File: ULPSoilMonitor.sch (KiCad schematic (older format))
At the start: 36 parts, among them J1 Conn_01x03_Male, J2 Conn_01x03_Male, J3 Conn_01x03_Male, J4 Conn_01x03_Male, J5 Conn_01x03_Male, J6 Conn_01x03_Male, J7 USB_B_Micro, Q1 BC807, Q2 MMDT3904, U1 ESP32-WROOM-32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

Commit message: fix cap unit of measure
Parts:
- C3: value 100μF -> 100nF
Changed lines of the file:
@@
 P 2600 1550
 F 0 "C3" H 2715 1596 50  0000 L CNN
-F 1 "100μF" H 2715 1505 50  0000 L CNN
+F 1 "100nF" H 2715 1505 50  0000 L CNN
 F 2 "Capacitors_SMD:C_0805" H 2638 1400 50  0001 C CNN
 F 3 "~" H 2600 1550 50  0001 C CNN

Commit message: update to use 18650 LiFePO4 cells
* connectors for one or two 18650 cells
* jumper to switch between battery & USB power
* add optional BME380
* reset push button
* more caps
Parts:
- removed C4: 100nF, Capacitors_SMD:C_0805, symbol Device:C
- removed J1, J2, J3, J4, J5, J6: Conn_01x03_Male, Pin_Headers:Pin_Header_Straight_1x03_Pitch2.54mm, symbol Connector:Conn_01x03_Male
- removed J7: USB_B_Micro, Connect:USB_Micro-B, symbol Connector:USB_B_Micro
- removed Q1: BC807, TO_SOT_Packages_SMD:SOT-23, symbol Transistor_BJT:BC807
- removed Q2: MMDT3904, TO_SOT_Packages_SMD:SOT-363_SC-70-6, symbol Transistor_BJT:MMDT3904
- removed R1, R11, R14, R5, R7, R9: 68k, Resistors_SMD:R_0805, symbol Device:R
- removed R10, R12, R15, R4, R6, R8: 30k, Resistors_SMD:R_0805, symbol Device:R
- removed R16: 3k9, Resistors_SMD:R_0805, symbol Device:R
- removed R17, R18: 10k, Resistors_SMD:R_0805, symbol Device:R
- removed R19, R20: 27R, Resistors_SMD:R_0805, symbol Device:R
- removed U2: FT231XS, Housings_SSOP:QSOP-20_3.9x8.7mm_Pitch0.635mm, symbol Interface_USB:FT231XS
- added C1: 470μF, Capacitor_SMD:CP_Elec_6.3x7.7, symbol Device:CP
- added C5: 330nF, Capacitor_SMD:C_0805_2012Metric, symbol Device:C
- added C6: 100nF, Capacitor_SMD:C_0805_2012Metric, symbol Device:C
- added JP1: Jumper_3_Bridged12, Connector_PinHeader_2.54mm:PinHeader_1x03_P2.54mm_Vertical, symbol Jumper:Jumper_3_Bridged12
- added SW1: RESET, Button_Switch_SMD:SW_SPST_FSMSM, symbol Switch:SW_Push
- added U2: UA7BM33, Package_TO_SOT_SMD:SOT-223-3_TabPin2, symbol Regulator_Linear:LM2937xMP
- BT1: footprint flobs-KiCad-footprints:BH321-2P -> flobs-KiCad-footprints:BatteryHolder_BHC-18650-1P-2P
- C2: renamed from C1; footprint Capacitors_SMD:C_0805 -> Capacitor_SMD:C_0805_2012Metric
- C3: renamed from C2; footprint Capacitors_SMD:C_0805 -> Capacitor_SMD:C_0805_2012Metric
- C4: renamed from C3; footprint Capacitors_SMD:C_0805 -> Capacitor_SMD:C_0805_2012Metric
- R1: renamed from R13; footprint Resistors_SMD:R_0805 -> Resistor_SMD:R_0805_2012Metric
- R2: value 30k -> 4k7; footprint Resistors_SMD:R_0805 -> Resistor_SMD:R_0805_2012Metric
- R3: value 68k -> 4k7; footprint Resistors_SMD:R_0805 -> Resistor_SMD:R_0805_2012Metric
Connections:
- net labels added: +3V3, SCL, SDA, VCC, VCC_SCALED
- net labels removed: BATT_SCALED, D+, D-, SENSOR0, SENSOR1, SENSOR2, SENSOR3, SENSOR4, SENSOR5, SENSOR_VCC
- wire segments 150 -> 95
- no-connect marks 30 -> 27
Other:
- moved on the sheet: BT1, C2, C3, C4, R1

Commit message: change USB to Serial chip, support charging
* exchanges FTDI FT231X for SILabs CP2102N
* adds MicroChip MCP73123 for LiFePO4 charging
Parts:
- removed C5: 330nF, Capacitor_SMD:C_0805_2012Metric, symbol Device:C
- removed C6: 100nF, Capacitor_SMD:C_0805_2012Metric, symbol Device:C
- removed JP1: Jumper_3_Bridged12, Connector_PinHeader_2.54mm:PinHeader_1x03_P2.54mm_Vertical, symbol Jumper:Jumper_3_Bridged12
- removed U2: UA7BM33, Package_TO_SOT_SMD:SOT-223-3_TabPin2, symbol Regulator_Linear:LM2937xMP
- added C?: 4.7μF, symbol Device:C
- added D?: CHARGING, symbol Device:LED
- added Q? (x2): MMDT3904, Package_TO_SOT_SMD:SOT-363_SC-70-6, symbol Transistor_BJT:MMDT3904
- added Q?: BC817, Package_TO_SOT_SMD:SOT-23, symbol Transistor_BJT:BC817
- added R?: 1k, symbol Device:R
- added R?: 2k37, symbol Device:R
- added R?: 3k9, symbol Device:R
- added U?: MCP73123, Package_DFN_QFN:DFN-10-1EP_3x3mm_P0.5mm_EP1.65x2.38mm_ThermalVias, symbol flobs-KiCad-lib:MCP73123
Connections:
- net labels added: CHR0, CHR1, CHREN, PROG
- net labels removed: +3V3
- wire segments 95 -> 117
- no-connect marks 27 -> 34

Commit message: update drawing to 882a528a10f6fb48f6454efd446c1280f51ad1f8
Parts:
- C5: renamed from C?; footprint (none) -> Capacitor_SMD:C_0805_2012Metric
- D1: renamed from D?; footprint (none) -> LED_SMD:LED_0805_2012Metric
- R23, R24, R25: renamed from R?; footprint (none) -> Resistor_SMD:R_0805_2012Metric
- U2: renamed from U?; footprint Package_DFN_QFN:DFN-10-1EP_3x3mm_P0.5mm_EP1.65x2.38mm_ThermalVias -> Package_DFN_QFN:DFN-10-1EP_3x3mm_P0.5mm_EP1.65x2.38mm
- gave numbers to parts that had none: 2
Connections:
- wire segments 117 -> 119
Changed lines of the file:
@@
 Sheet 1 5
 Title "ULPSoilMonitor"
-Date "2020-05-16"
-Rev "v2.0"
+Date "2020-06-26"
+Rev "v2.1"
 Comp "Flobs"
 Comment1 ""
@@
 Wire Wire Line
 	2350 1050 2350 1150
-Wire Wire Line
-	2150 1050 2150 900
 Connection ~ 2150 1050
 Wire Wire Line
@@
 	5700 1250 5850 1250
 Wire Wire Line
-	1950 1050 1500 1050
+	1950 1050 1750 1050
 Wire Wire Line
 	1500 1050 1500 1150
@@
 	4500 5300 4600 5300
 $Comp
-L flobs-KiCad-lib:MCP73123 U?
+L flobs-KiCad-lib:MCP73123 U2
 U 1 1 5EFBF713
 P 7400 5400
-F 0 "U?" H 7400 5915 50  0000 C CNN
+F 0 "U2" H 7400 5915 50  0000 C CNN
 F 1 "MCP73123" H 7400 5824 50  0000 C CNN
-F 2 "Package_DFN_QFN:DFN-10-1EP_3x3mm_P0.5mm_EP1.65x2.38mm_ThermalVias" H 7050 6200 50  0001 C CNN
+F 2 "Package_DFN_QFN:DFN-10-1EP_3x3mm_P0.5mm_EP1.65x2.38mm" H 7050 6200 50  0001 C CNN
 F 3 "" H 7050 6200 50  0001 C CNN
 	1    7400 5400
@@
 $EndComp
 $Comp
-L power:GND #PWR?
+L power:GND #PWR0101
 U 1 1 5EFC114A
 P 7400 6250
-F 0 "#PWR?" H 7400 6000 50  0001 C CNN
+F 0 "#PWR0101" H 7400 6000 50  0001 C CNN
 F 1 "GND" H 7405 6077 50  0000 C CNN
 F 2 "" H 7400 6250 50  0001 C CNN
@@
 $EndComp
 $Comp
-L power:GND #PWR?
+L power:GND #PWR0102
 U 1 1 5EFC14F0
 P 8050 5800
-F 0 "#PWR?" H 8050 5550 50  0001 C CNN
+F 0 "#PWR0102" H 8050 5550 50  0001 C CNN
 F 1 "GND" H 8055 5627 50  0000 C CNN
 F 2 "" H 8050 5800 50  0001 C CNN
@@
 Connection ~ 8050 5450
 $Comp
-L power:+BATT #PWR?
+L power:+BATT #PWR0103
 U 1 1 5EFC7B48
 P 6550 5000
-F 0 "#PWR?" H 6550 4850 50  0001 C CNN
+F 0 "#PWR0103" H 6550 4850 50  0001 C CNN
 F 1 "+BATT" H 6565 5173 50  0000 C CNN
 F 2 "" H 6550 5000 50  0001 C CNN
@@
 $EndComp
 $Comp
-L power:VBUS #PWR?
+L power:VBUS #PWR0104
 U 1 1 5EFC869F
 P 6750 4900
-F 0 "#PWR?" H 6750 4750 50  0001 C CNN
+F 0 "#PWR0104" H 6750 4750 50  0001 C CNN
 F 1 "VBUS" H 6765 5073 50  0000 C CNN
 F 2 "" H 6750 4900 50  0001 C CNN
@@
 	7900 5450 8050 5450
 $Comp
-L Device:LED D?
+L Device:LED D1
 U 1 1 5EFE3865
 P 8300 5350
-F 0 "D?" V 8339 5232 50  0000 R CNN
+F 0 "D1" V 8339 5232 50  0000 R CNN
 F 1 "CHARGING" V 8248 5232 50  0000 R CNN
-F 2 "" H 8300 5350 50  0001 C CNN
+F 2 "LED_SMD:LED_0805_2012Metric" H 8300 5350 50  0001 C CNN
 F 3 "~" H 8300 5350 50  0001 C CNN
 	1    8300 5350
@@
 $EndComp
 $Comp
-L Device:R R?
+L Device:R R23
 U 1 1 5EFE4E96
 P 8300 4900
-F 0 "R?" H 8370 4946 50  0000 L CNN
+F 0 "R23" H 8370 4946 50  0000 L CNN
 F 1 "1k" H 8370 4855 50  0000 L CNN
-F 2 "" V 8230 4900 50  0001 C CNN
+F 2 "Resistor_SMD:R_0805_2012Metric" V 8230 4900 50  0001 C CNN
 F 3 "~" H 8300 4900 50  0001 C CNN
 	1    8300 4900
@@
 	8300 5200 8300 5050
 $Comp
-L power:VBUS #PWR?
+L power:VBUS #PWR0105
 U 1 1 5EFEC5B1
 P 8300 4650
-F 0 "#PWR?" H 8300 4500 50  0001 C CNN
+F 0 "#PWR0105" H 8300 4500 50  0001 C CNN
 F 1 "VBUS" H 8315 4823 50  0000 C CNN
 F 2 "" H 8300 4650 50  0001 C CNN
@@
 	8300 4750 8300 4650
 $Comp
-L Device:C C?
+L Device:C C5
 U 1 1 5EFF0D8F
 P 6550 5900
-F 0 "C?" H 6665 5946 50  0000 L CNN
+F 0 "C5" H 6665 5946 50  0000 L CNN
 F 1 "4.7μF" H 6665 5855 50  0000 L CNN
-F 2 "" H 6588 5750 50  0001 C CNN
+F 2 "Capacitor_SMD:C_0805_2012Metric" H 6588 5750 50  0001 C CNN
 F 3 "~" H 6550 5900 50  0001 C CNN
 	1    6550 5900
@@
 	6550 6050 6550 6250
 $Comp
-L power:GND #PWR?
+L power:GND #PWR0106
 U 1 1 5EFF8A21
 P 6550 6250
-F 0 "#PWR?" H 6550 6000 50  0001 C CNN
+F 0 "#PWR0106" H 6550 6000 50  0001 C CNN
 F 1 "GND" H 6555 6077 50  0000 C CNN
 F 2 "" H 6550 6250 50  0001 C CNN
@@
 	7900 5150 8000 5150
 $Comp
-L Device:R R?
+L Device:R R25
 U 1 1 5F015CC3
 P 9900 5350
-F 0 "R?" H 9970 5396 50  0000 L CNN
+F 0 "R25" H 9970 5396 50  0000 L CNN
 F 1 "2k37" H 9970 5305 50  0000 L CNN
-F 2 "" V 9830 5350 50  0001 C CNN
+F 2 "Resistor_SMD:R_0805_2012Metric" V 9830 5350 50  0001 C CNN
 F 3 "~" H 9900 5350 50  0001 C CNN
 	1    9900 5350
@@
 $EndComp
 $Comp
-L Transistor_BJT:MMDT3904 Q?
+L Transistor_BJT:MMDT3904 Q4
 U 1 1 5F018C0F
 P 9500 5600
-F 0 "Q?" H 9691 5646 50  0000 L CNN
+F 0 "Q4" H 9691 5646 50  0000 L CNN
 F 1 "MMDT3904" H 9691 5555 50  0000 L CNN
 F 2 "Package_TO_SOT_SMD:SOT-363_SC-70-6" H 9700 5700 50  0001 C CNN
@@
 $EndComp
 $Comp
-L Transistor_BJT:MMDT3904 Q?
+L Transistor_BJT:MMDT3904 Q4
 U 2 1 5F019AA5
 P 10000 5900
-F 0 "Q?" H 10191 5946 50  0000 L CNN
+F 0 "Q4" H 10191 5946 50  0000 L CNN
 F 1 "MMDT3904" H 10191 5855 50  0000 L CNN
 F 2 "Package_TO_SOT_SMD:SOT-363_SC-70-6" H 10200 6000 50  0001 C CNN
@@
 CHR0
 $Comp
-L Device:R R?
+L Device:R R24
 U 1 1 5F02346F
 P 9400 5150
-F 0 "R?" H 9470 5196 50  0000 L CNN
+F 0 "R24" H 9470 5196 50  0000 L CNN
 F 1 "3k9" H 9470 5105 50  0000 L CNN
-F 2 "" V 9330 5150 50  0001 C CNN
+F 2 "Resistor_SMD:R_0805_2012Metric" V 9330 5150 50  0001 C CNN
 F 3 "~" H 9400 5150 50  0001 C CNN
 	1    9400 5150
@@
 CHR1
 $Comp
-L power:GND #PWR?
+L power:GND #PWR0107
 U 1 1 5F02E788
 P 9650 6300
-F 0 "#PWR?" H 9650 6050 50  0001 C CNN
+F 0 "#PWR0107" H 9650 6050 50  0001 C CNN
 F 1 "GND" H 9655 6127 50  0000 C CNN
 F 2 "" H 9650 6300 50  0001 C CNN
@@
 	9700 5600 10300 5600
 $Comp
-L Transistor_BJT:BC817 Q?
+L Transistor_BJT:BC817 Q3
 U 1 1 5F0D63E8
 P 9750 4600
-F 0 "Q?" H 9941 4646 50  0000 L CNN
+F 0 "Q3" H 9941 4646 50  0000 L CNN
 F 1 "BC817" H 9941 4555 50  0000 L CNN
 F 2 "Package_TO_SOT_SMD:SOT-23" H 9950 4525 50  0001 L CIN
@@
 Wire Wire Line
 	9950 4600 10050 4600
+$Comp
+L power:+BATT #PWR0112
+U 1 1 5EF7A415
+P 1750 900
+F 0 "#PWR0112" H 1750 750 50  0001 C CNN
+F 1 "+BATT" H 1765 1073 50  0000 C CNN
+F 2 "" H 1750 900 50  0001 C CNN
+F 3 "" H 1750 900 50  0001 C CNN
+	1    1750 900
+	1    0    0    -1
+$EndComp
+Wire Wire Line
+	2150 900  2150 1050
+Wire Wire Line
+	1750 900  1750 1050
+Connection ~ 1750 1050
+Wire Wire Line
+	1750 1050 1500 1050
 $EndSCHEMATC

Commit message: Add JCLPCB/LCSC part numbers
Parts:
- C1: LCSC (none) -> C335982
- C2: LCSC (none) -> C45783
- C3, C4: LCSC (none) -> C49678
- C5: LCSC (none) -> C1779
- D1: LCSC (none) -> C84256
- Q3: LCSC (none) -> C118725
- Q4: LCSC (none) -> C155305
- R1: LCSC (none) -> C17414
- R2, R3: LCSC (none) -> C17673
- R23: LCSC (none) -> C17513
- R24: LCSC (none) -> C17614
- R25: LCSC (none) -> C17523
- SW1: LCSC (none) -> C354943
- U1: symbol RF_Module:ESP32-WROOM-32 -> ULPSoilMonitor-rescue:ESP32-WROOM-32-RF_Module; LCSC (none) -> C473012
- U2: symbol flobs-KiCad-lib:MCP73123 -> ULPSoilMonitor-rescue:MCP73123-flobs-KiCad-lib
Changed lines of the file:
@@
 EESchema Schematic File Version 4
+LIBS:ULPSoilMonitor-cache
 EELAYER 30 0
 EELAYER END
@@
 F 2 "Resistor_SMD:R_0805_2012Metric" V 3530 2750 50  0001 C CNN
 F 3 "~" H 3600 2750 50  0001 C CNN
+F 4 "C17673" H 3600 2750 50  0001 C CNN "LCSC"
 	1    3600 2750
 	0    1    1    0
@@
 F 2 "Resistor_SMD:R_0805_2012Metric" V 3530 2950 50  0001 C CNN
 F 3 "~" H 3600 2950 50  0001 C CNN
+F 4 "C17673" H 3600 2950 50  0001 C CNN "LCSC"
 	1    3600 2950
 	0    1    1    0
@@
 F 2 "Capacitor_SMD:CP_Elec_6.3x7.7" H 1538 1150 50  0001 C CNN
 F 3 "~" H 1500 1300 50  0001 C CNN
+F 4 "C335982" H 1500 1300 50  0001 C CNN "LCSC"
 	1    1500 1300
 	1    0    0    -1
@@
 F 2 "Capacitor_SMD:C_0805_2012Metric" H 3038 1400 50  0001 C CNN
 F 3 "~" H 3000 1550 50  0001 C CNN
+F 4 "C49678" H 3000 1550 50  0001 C CNN "LCSC"
 	1    3000 1550
 	1    0    0    -1
@@
 F 2 "Resistor_SMD:R_0805_2012Metric" V 2930 1050 50  0001 C CNN
 F 3 "~" H 3000 1050 50  0001 C CNN
+F 4 "C17414" H 3000 1050 50  0001 C CNN "LCSC"
 	1    3000 1050
 	1    0    0    -1
@@
 F 2 "Capacitor_SMD:C_0805_2012Metric" H 2388 1150 50  0001 C CNN
 F 3 "~" H 2350 1300 50  0001 C CNN
+F 4 "C49678" H 2350 1300 50  0001 C CNN "LCSC"
 	1    2350 1300
 	1    0    0    -1
@@
 F 2 "Capacitor_SMD:C_0805_2012Metric" H 1988 1150 50  0001 C CNN
 F 3 "~" H 1950 1300 50  0001 C CNN
+F 4 "C45783" H 1950 1300 50  0001 C CNN "LCSC"
 	1    1950 1300
 	1    0    0    -1
@@
 $EndComp
 $Comp
-L RF_Module:ESP32-WROOM-32 U1
+L ULPSoilMonitor-rescue:ESP32-WROOM-32-RF_Module U1
 U 1 1 5E9ED41E
 P 5100 2450
@@
 F 2 "RF_Module:ESP32-WROOM-32" H 5100 950 50  0001 C CNN
 F 3 "https://www.espressif.com/sites/default/files/documentation/esp32-wroom-32_datasheet_en.pdf" H 4800 2500 50  0001 C CNN
+F 4 "C473012" H 5100 2450 50  0001 C CNN "LCSC"
 	1    5100 2450
 	1    0    0    -1
@@
 F 2 "Button_Switch_SMD:SW_SPST_FSMSM" H 6650 1500 50  0001 C CNN
 F 3 "~" H 6650 1500 50  0001 C CNN
+F 4 "C354943" V 6650 1300 50  0001 C CNN "LCSC"
 	1    6650 1300
 	0    1    1    0
@@
 	4500 5300 4600 5300
 $Comp
-L flobs-KiCad-lib:MCP73123 U2
+L ULPSoilMonitor-rescue:MCP73123-flobs-KiCad-lib U2
 U 1 1 5EFBF713
 P 7400 5400
@@
 F 2 "LED_SMD:LED_0805_2012Metric" H 8300 5350 50  0001 C CNN
 F 3 "~" H 8300 5350 50  0001 C CNN
+F 4 "C84256" H 8300 5350 50  0001 C CNN "LCSC"
 	1    8300 5350
 	0    -1   -1   0
@@
 F 2 "Resistor_SMD:R_0805_2012Metric" V 8230 4900 50  0001 C CNN
 F 3 "~" H 8300 4900 50  0001 C CNN
+F 4 "C17513" H 8300 4900 50  0001 C CNN "LCSC"
 	1    8300 4900
 	1    0    0    -1
@@
 F 2 "Capacitor_SMD:C_0805_2012Metric" H 6588 5750 50  0001 C CNN
 F 3 "~" H 6550 5900 50  0001 C CNN
+F 4 "C1779" H 6550 5900 50  0001 C CNN "LCSC"
 	1    6550 5900
 	1    0    0    -1
@@
 F 2 "Resistor_SMD:R_0805_2012Metric" V 9830 5350 50  0001 C CNN
 F 3 "~" H 9900 5350 50  0001 C CNN
+F 4 "C17523" H 9900 5350 50  0001 C CNN "LCSC"
 	1    9900 5350
 	1    0    0    -1
@@
 F 2 "Package_TO_SOT_SMD:SOT-363_SC-70-6" H 9700 5700 50  0001 C CNN
 F 3 "http://www.diodes.com/_files/datasheets/ds30088.pdf" H 9500 5600 50  0001 C CNN
+F 4 "C155305" H 9500 5600 50  0001 C CNN "LCSC"
 	1    9500 5600
 	-1   0    0    -1
@@
 F 2 "Package_TO_SOT_SMD:SOT-363_SC-70-6" H 10200 6000 50  0001 C CNN
 F 3 "http://www.diodes.com/_files/datasheets/ds30088.pdf" H 10000 5900 50  0001 C CNN
+F 4 "C155305" H 10000 5900 50  0001 C CNN "LCSC"
 	2    10000 5900
 	-1   0    0    -1
@@
 F 2 "Resistor_SMD:R_0805_2012Metric" V 9330 5150 50  0001 C CNN
 F 3 "~" H 9400 5150 50  0001 C CNN
+F 4 "C17614" H 9400 5150 50  0001 C CNN "LCSC"
 	1    9400 5150
 	1    0    0    -1
@@
 F 2 "Package_TO_SOT_SMD:SOT-23" H 9950 4525 50  0001 L CIN
 F 3 "http://www.fairchildsemi.com/ds/BC/BC817.pdf" H 9750 4600 50  0001 L CNN
+F 4 "C118725" H 9750 4600 50  0001 C CNN "LCSC"
 	1    9750 4600
 	-1   0    0    -1

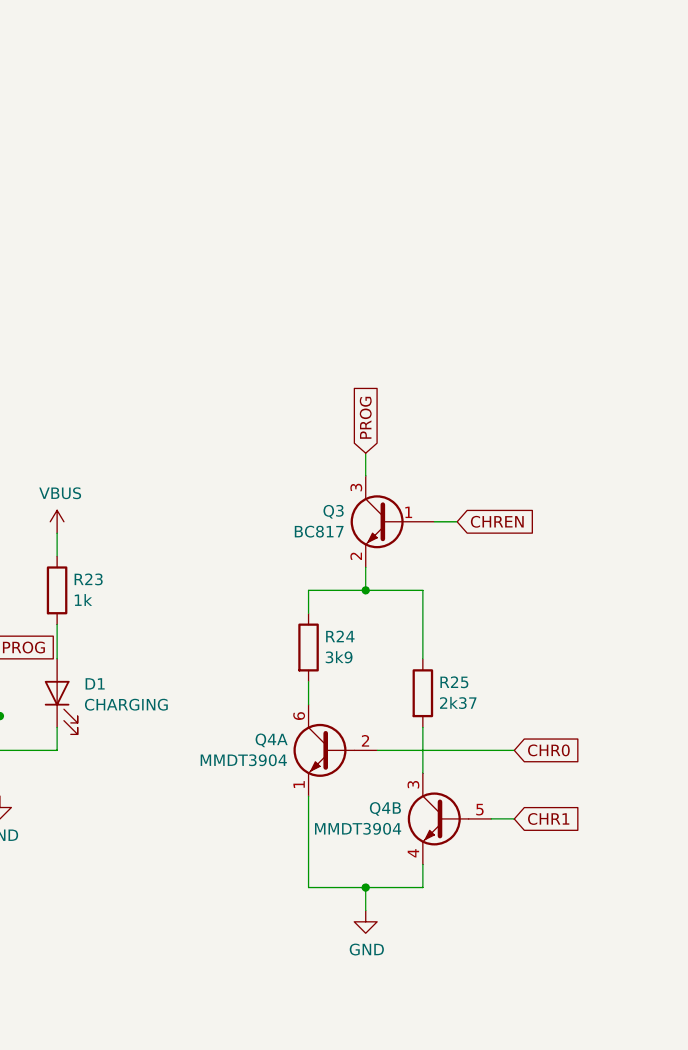
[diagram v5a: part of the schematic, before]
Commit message: Set USB-serial DNP
Disable USB-serial
Add switches for LiFePo charger PROG setting
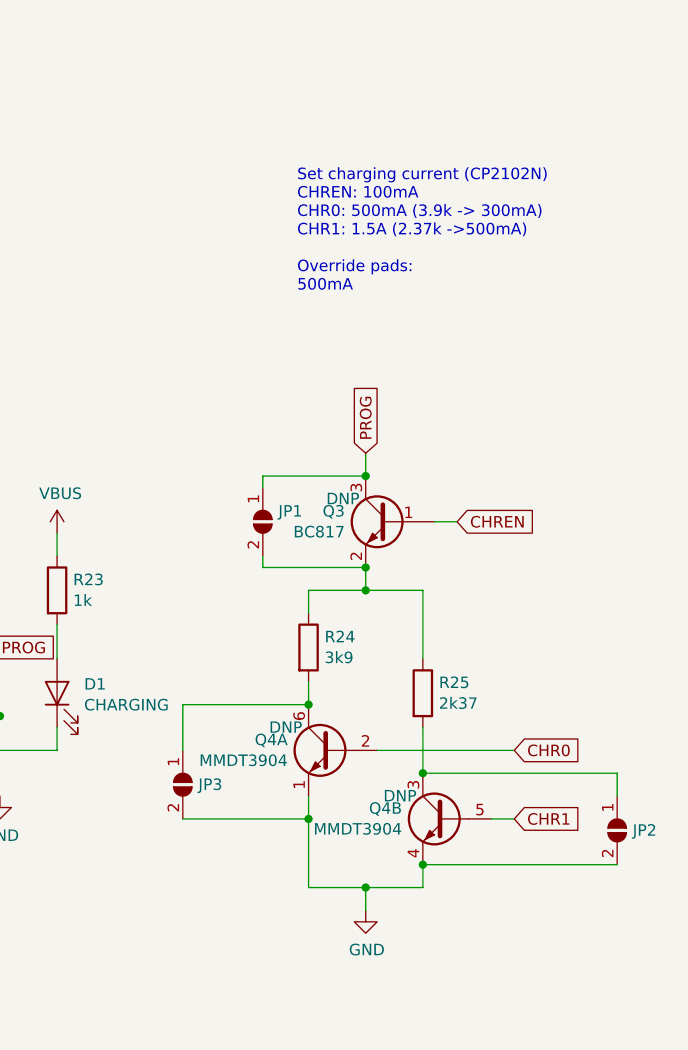
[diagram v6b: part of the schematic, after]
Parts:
- added JP1, JP2, JP3: SolderJumper_2_Open, Jumper:SolderJumper-2_P1.3mm_Open_RoundedPad1.0x1.5mm, symbol 0-GIE_SMD_Jumpers:SolderJumper_2_Open
- Q3, Q4: DNP (none) -> DNP
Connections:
- net -BATT: now also JP2.2 (B), JP3.2 (B)
- net PROG: now also JP1.1 (A)
- net at Q3.2 (E), R24.1, R25.1: now also JP1.2 (B)
- net at Q4.3 (C2), R25.2: now also JP2.1 (A)
- net at Q4.6 (C1), R24.2: now also JP3.1 (A)
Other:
- note added: "Set charging current (CP2102N)\nCHREN: 100mA\nCHR0: 500mA (3.9k -> 300mA)\nCHR1: 1.5A (2.37k ->500mA)\n\nOverride pads: \n500mA"
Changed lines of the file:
@@
 F 3 "http://www.diodes.com/_files/datasheets/ds30088.pdf" H 9500 5600 50  0001 C CNN
 F 4 "C155305" H 9500 5600 50  0001 C CNN "LCSC"
+F 5 "DNP" H 9700 5700 50  0000 C CNN "DNP"
 	1    9500 5600
 	-1   0    0    -1
@@
 F 3 "http://www.diodes.com/_files/datasheets/ds30088.pdf" H 10000 5900 50  0001 C CNN
 F 4 "C155305" H 10000 5900 50  0001 C CNN "LCSC"
+F 5 "DNP" H 10200 6000 50  0000 C CNN "DNP"
 	2    10000 5900
 	-1   0    0    -1
@@
 Text GLabel 10300 5600 2    50   Input ~ 0
 CHR0
-$Comp
-L Device:R R24
-U 1 1 5F02346F
-P 9400 5150
-F 0 "R24" H 9470 5196 50  0000 L CNN
-F 1 "3k9" H 9470 5105 50  0000 L CNN
-F 2 "Resistor_SMD:R_0805_2012Metric" V 9330 5150 50  0001 C CNN
-F 3 "~" H 9400 5150 50  0001 C CNN
-F 4 "C17614" H 9400 5150 50  0001 C CNN "LCSC"
-	1    9400 5150
-	1    0    0    -1
-$EndComp
 Text GLabel 10300 5900 2    50   Input ~ 0
 CHR1
@@
 $EndComp
 Wire Wire Line
-	9400 5800 9400 6200
+	9400 5800 9400 5900
 Wire Wire Line
 	9400 6200 9650 6200
@@
 F 3 "http://www.fairchildsemi.com/ds/BC/BC817.pdf" H 9750 4600 50  0001 L CNN
 F 4 "C118725" H 9750 4600 50  0001 C CNN "LCSC"
+F 5 "DNP" H 9950 4700 50  0000 C CNN "DNP"
 	1    9750 4600
 	-1   0    0    -1
@@
 Wire Wire Line
 	1750 1050 1500 1050
+Text Notes 9350 3600 0    50   ~ 0
+Set charging current (CP2102N)\nCHREN: 100mA\nCHR0: 500mA (3.9k -> 300mA)\nCHR1: 1.5A (2.37k ->500mA)\n\nOverride pads: \n500mA
+$Comp
+L 0-GIE_SMD_Jumpers:SolderJumper_2_Open JP1
+U 1 1 605B68DB
+P 9200 4600
+F 0 "JP1" V 9154 4668 50  0000 L CNN
+F 1 "SolderJumper_2_Open" V 9245 4668 50  0001 L CNN
+F 2 "Jumper:SolderJumper-2_P1.3mm_Open_RoundedPad1.0x1.5mm" H 9200 4600 50  0001 C CNN
+F 3 "~" H 9200 4600 50  0001 C CNN
+	1    9200 4600
+	0    1    1    0
+$EndComp
+$Comp
+L 0-GIE_SMD_Jumpers:SolderJumper_2_Open JP2
+U 1 1 605B8584
+P 10750 5950
+F 0 "JP2" V 10750 6018 50  0000 L CNN
+F 1 "SolderJumper_2_Open" V 10795 6018 50  0001 L CNN
+F 2 "Jumper:SolderJumper-2_P1.3mm_Open_RoundedPad1.0x1.5mm" H 10750 5950 50  0001 C CNN
+F 3 "~" H 10750 5950 50  0001 C CNN
+	1    10750 5950
+	0    1    1    0
+$EndComp
+Wire Wire Line
+	9650 4400 9200 4400
+Wire Wire Line
+	9200 4400 9200 4450
+Connection ~ 9650 4400
+Wire Wire Line
+	9200 4750 9200 4800
+Wire Wire Line
+	9200 4800 9650 4800
+Connection ~ 9650 4800
+Wire Wire Line
+	10750 5800 10750 5700
+Wire Wire Line
+	10750 5700 9900 5700
+Connection ~ 9900 5700
+Wire Wire Line
+	9900 6100 10750 6100
+Connection ~ 9900 6100
+$Comp
+L Device:R R24
+U 1 1 5F02346F
+P 9400 5150
+F 0 "R24" H 9470 5196 50  0000 L CNN
+F 1 "3k9" H 9470 5105 50  0000 L CNN
+F 2 "Resistor_SMD:R_0805_2012Metric" V 9330 5150 50  0001 C CNN
+F 3 "~" H 9400 5150 50  0001 C CNN
+F 4 "C17614" H 9400 5150 50  0001 C CNN "LCSC"
+	1    9400 5150
+	1    0    0    -1
+$EndComp
+$Comp
+L 0-GIE_SMD_Jumpers:SolderJumper_2_Open JP3
+U 1 1 605D5828
+P 8850 5750
+F 0 "JP3" V 8850 5818 50  0000 L CNN
+F 1 "SolderJumper_2_Open" V 8895 5818 50  0001 L CNN
+F 2 "Jumper:SolderJumper-2_P1.3mm_Open_RoundedPad1.0x1.5mm" H 8850 5750 50  0001 C CNN
+F 3 "~" H 8850 5750 50  0001 C CNN
+	1    8850 5750
+	0    1    1    0
+$EndComp
+Wire Wire Line
+	8850 5600 8850 5400
+Wire Wire Line
+	8850 5400 9400 5400
+Connection ~ 9400 5400
+Wire Wire Line
+	8850 5900 9400 5900
+Connection ~ 9400 5900
+Wire Wire Line
+	9400 5900 9400 6200
 $EndSCHEMATC

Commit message: Update jumper names
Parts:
- JP1: value SolderJumper_2_Open -> Charg_enable
- JP2: value SolderJumper_2_Open -> Charge_500mA
- JP3: value SolderJumper_2_Open -> Charge_300mA
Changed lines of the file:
@@
 P 9200 4600
 F 0 "JP1" V 9154 4668 50  0000 L CNN
-F 1 "SolderJumper_2_Open" V 9245 4668 50  0001 L CNN
+F 1 "Charg_enable" V 9245 4668 50  0001 L CNN
 F 2 "Jumper:SolderJumper-2_P1.3mm_Open_RoundedPad1.0x1.5mm" H 9200 4600 50  0001 C CNN
 F 3 "~" H 9200 4600 50  0001 C CNN
@@
 P 10750 5950
 F 0 "JP2" V 10750 6018 50  0000 L CNN
-F 1 "SolderJumper_2_Open" V 10795 6018 50  0001 L CNN
+F 1 "Charge_500mA" V 10795 6018 50  0001 L CNN
 F 2 "Jumper:SolderJumper-2_P1.3mm_Open_RoundedPad1.0x1.5mm" H 10750 5950 50  0001 C CNN
 F 3 "~" H 10750 5950 50  0001 C CNN
@@
 P 8850 5750
 F 0 "JP3" V 8850 5818 50  0000 L CNN
-F 1 "SolderJumper_2_Open" V 8895 5818 50  0001 L CNN
+F 1 "Charge_300mA" V 8895 5818 50  0001 L CNN
 F 2 "Jumper:SolderJumper-2_P1.3mm_Open_RoundedPad1.0x1.5mm" H 8850 5750 50  0001 C CNN
 F 3 "~" H 8850 5750 50  0001 C CNN
